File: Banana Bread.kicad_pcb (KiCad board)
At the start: 2 copper layers, 26 x 32 mm, 9 parts, among them J1 Conn_01x01_MountingPin, J2 Conn_02x04_Top_Bottom

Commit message: make copper fill clearance consistent
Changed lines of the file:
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@@
   )
   (zone locked (net 2) (net_name "unconnected-(J1-PadMP)") (layers F&B.Cu) (hatch edge 0.508)
-    (connect_pads yes (clearance 0.508))
-    (min_thickness 0.254) (filled_areas_thickness no)
+    (connect_pads yes (clearance 0.35))
+    (min_thickness 0.127) (filled_areas_thickness no)
     (fill yes (thermal_gap 0.508) (thermal_bridge_width 0.508))
     (polygon
@@
     )
   )
-  (zone locked (net 1) (net_name "Net-(J1-Pad1)") (layer "F.Cu") (hatch edge 0.508)
+  (zone locked (net 1) (net_name "Net-(J1-Pad1)") (layers F&B.Cu) (hatch edge 0.508)
     (priority 1)
-    (connect_pads yes (clearance 0.508))
-    (min_thickness 0.254) (filled_areas_thickness no)
+    (connect_pads yes (clearance 0.35))
+    (min_thickness 0.127) (filled_areas_thickness no)
     (fill yes (thermal_gap 0.508) (thermal_bridge_width 0.508))
     (polygon
@@
         (xy 157 100.54)
         (xy 157 90)
-        (xy 158.095 90)
-        (xy 161.905 90)
+        (xy 158.73 90)
+        (xy 161.27 90)
       )
     )
@@
       )
     )
-  )
-  (zone locked (net 1) (net_name "Net-(J1-Pad1)") (layer "B.Cu") (hatch edge 0.508)
-    (priority 1)
-    (connect_pads yes (clearance 0.508))
-    (min_thickness 0.254) (filled_areas_thickness no)
-    (fill yes (thermal_gap 0.508) (thermal_bridge_width 0.508))
-    (polygon
-      (pts
-        (xy 163 90)
-        (xy 163 100.54)
-        (xy 165.08 100.54)
-        (xy 165.08 105.62)
-        (xy 154.92 105.62)
-        (xy 154.92 100.54)
-        (xy 157 100.54)
-        (xy 157 90)
-        (xy 158.73 90)
-        (xy 161.27 90)
-      )
-    )

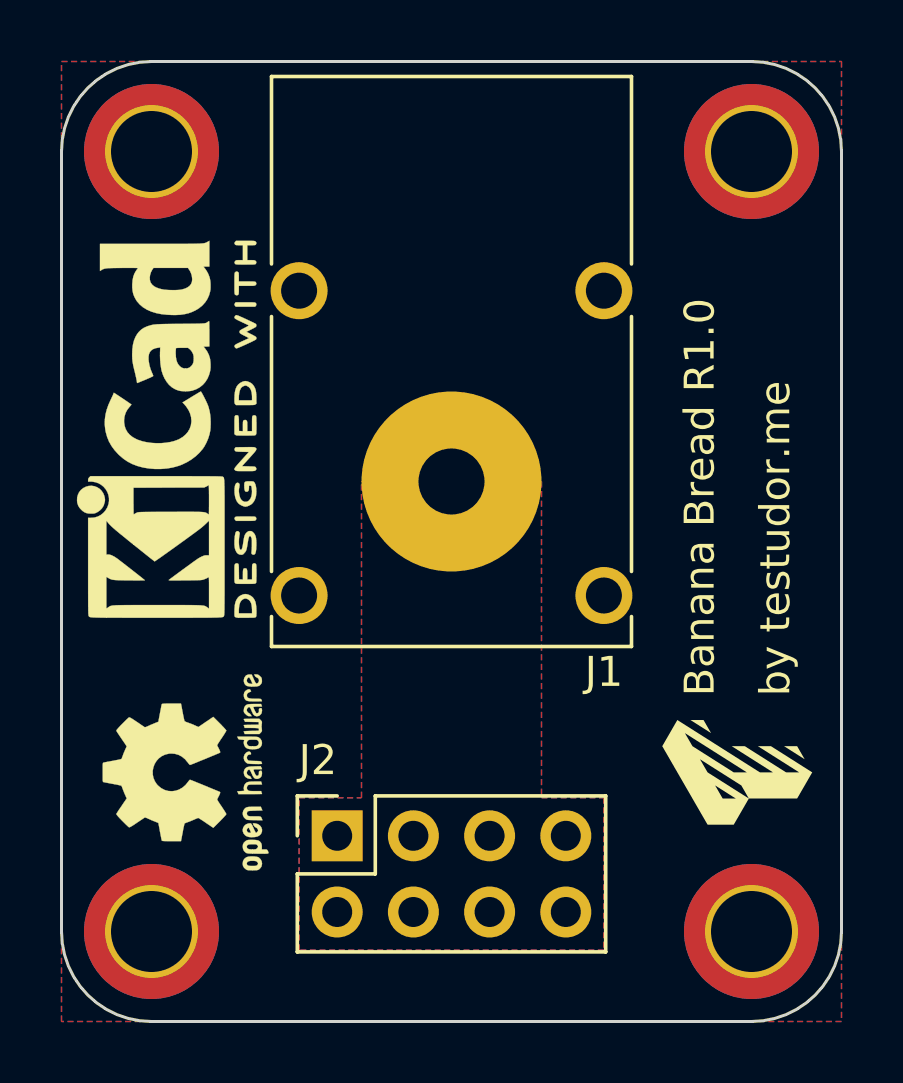
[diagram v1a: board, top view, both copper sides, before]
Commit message: make silkscreen consistent, add current rating
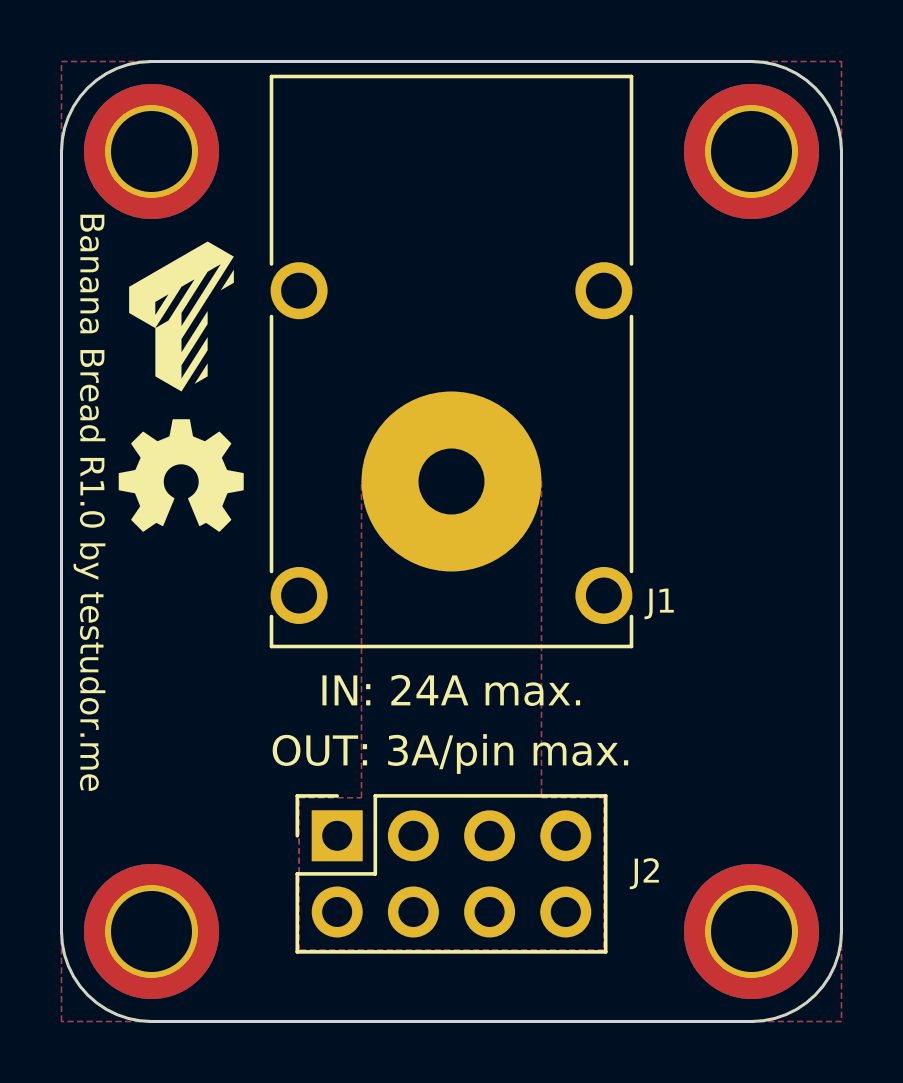
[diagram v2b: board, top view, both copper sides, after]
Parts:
- removed LOGO1: KiCad-Logo2_5mm_SilkScreen, Symbol:KiCad-Logo2_5mm_SilkScreen
- removed LOGO3: OSHW-Logo2_7.3x6mm_SilkScreen, Symbol:OSHW-Logo2_7.3x6mm_SilkScreen
- added REF**: OSHW-Symbol_5mm_SilkScreen, Custom_Symbols:OSHW-Symbol_5mm_SilkScreen, F.Cu at (151.0, 90.0)
- moved LOGO2 24.0 mm to (151.0, 84.5), turned to 0 degrees
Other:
- board text added: "Banana Bread R1.0 by testudor.me"
- board text added: "IN: 24A max."
- board text added: "OUT: 3A/pin max."
- board text removed: "Banana Bread R1.0"
- board text removed: "by testudor.me"

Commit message: Initial commit R1.1
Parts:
- added TP1: TestPoint_Probe, TestPoint:TestPoint_THTPad_D2.0mm_Drill1.0mm, F.Cu at (169.0, 88.0)
- added TP2: TestPoint_Probe, TestPoint:TestPoint_Pad_D2.0mm, F.Cu at (169.0, 93.0)
- added TP3: TestPoint_Probe, TestPoint:TestPoint_Keystone_5000-5004_Miniature, F.Cu at (169.0, 97.7)
- moved REF** 18.8 mm to (169.0, 84.5)
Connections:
- net Net-(J1-Pad1) renamed MAIN
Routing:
- net MAIN: track 0.00 -> 14.1 mm
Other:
- board text added: "Banana Bread R1.1 by testudor.me"
- board text removed: "Banana Bread R1.0 by testudor.me"

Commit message: Add final R1.1 changes
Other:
- board text added: "PCB3D_BR_BANANA-BREAD"
- board text added: "PCB3D_TL_BANANA-BREAD"
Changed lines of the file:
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@@
     (descr "Open Source Hardware Symbol")
     (tags "Logo Symbol OSHW")
-    (attr exclude_from_pos_files exclude_from_bom)
+    (attr board_only exclude_from_pos_files exclude_from_bom)
     (fp_text reference "REF**" (at 0 0) (layer "F.SilkS") hide
         (effects (font (size 1 1) (thickness 0.15)))
@@
     (effects (font (size 1 1) (thickness 0.15)))
   )
+  (gr_text "PCB3D_TL_BANANA-BREAD" (at 145 74) (layer "User.1")
+    (effects (font (size 0.5 0.5) (thickness 0.125) bold) (justify left bottom))
+  )
+  (gr_text "PCB3D_BR_BANANA-BREAD" (at 175 110) (layer "User.1")
+    (effects (font (size 0.5 0.5) (thickness 0.125) bold) (justify left bottom))
+  )
   (dimension locked (type aligned) (layer "Cmts.User")
